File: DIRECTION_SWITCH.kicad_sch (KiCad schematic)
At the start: 0 parts

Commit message: Layout + Schematic weiter gemacht
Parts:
- added SW1: SW_Omron_B3FS, Button_Switch_SMD:SW_SPST_Omron_B3FS-105xP, symbol Switch:SW_Omron_B3FS
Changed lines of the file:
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@@
 		(rev "Rev 1")
 	)
+	(symbol
+		(lib_id "Switch:SW_Omron_B3FS")
+		(at 125.73 73.66 0)
+		(unit 1)
+		(body_style 1)
+		(exclude_from_sim no)
+		(in_bom yes)
+		(on_board yes)
+		(in_pos_files yes)
+		(dnp no)
+		(fields_autoplaced yes)
+		(property "Reference" "SW1"
+			(at 125.73 66.04 0)
+			(show_name no)
+			(do_not_autoplace no)
+			(effects
+				(font
+					(size 1.27 1.27)
+				)
+			)
+		)
+		(property "Value" "SW_Omron_B3FS"
+			(at 125.73 68.58 0)
+			(show_name no)
+			(do_not_autoplace no)
+			(effects
+				(font
+					(size 1.27 1.27)
+				)
+			)
+		)
+		(property "Footprint" "Button_Switch_SMD:SW_SPST_Omron_B3FS-105xP"
+			(at 125.73 68.58 0)
+			(hide yes)
+			(show_name no)
+			(do_not_autoplace no)
+			(effects
+				(font
+					(size 1.27 1.27)
+				)
+			)
+		)
+		(property "Datasheet" "https://omronfs.omron.com/en_US/ecb/products/pdf/en-b3fs.pdf"
+			(at 125.73 68.58 0)
+			(hide yes)
+			(show_name no)
+			(do_not_autoplace no)
+			(effects
+				(font
+					(size 1.27 1.27)
+				)
+			)
+		)
+		(property "Description" "Omron B3FS 6x6mm single pole normally-open tactile switch"
+			(at 125.73 73.66 0)
+			(hide yes)
+			(show_name no)
+			(do_not_autoplace no)
+			(effects
+				(font
+					(size 1.27 1.27)
+				)
+			)
+		)
+		(pin "1"
+		)
+		(pin "2"
+		)
+		(instances
+			(project ""
+				(path "/96aa4cdc-6548-43b6-b96a-6d1618c17d83/d0a02d27-ba8e-47f5-91ea-312e7e888d13"
+					(reference "SW1")
+					(unit 1)
+				)
+			)
+		)
+	)
 )

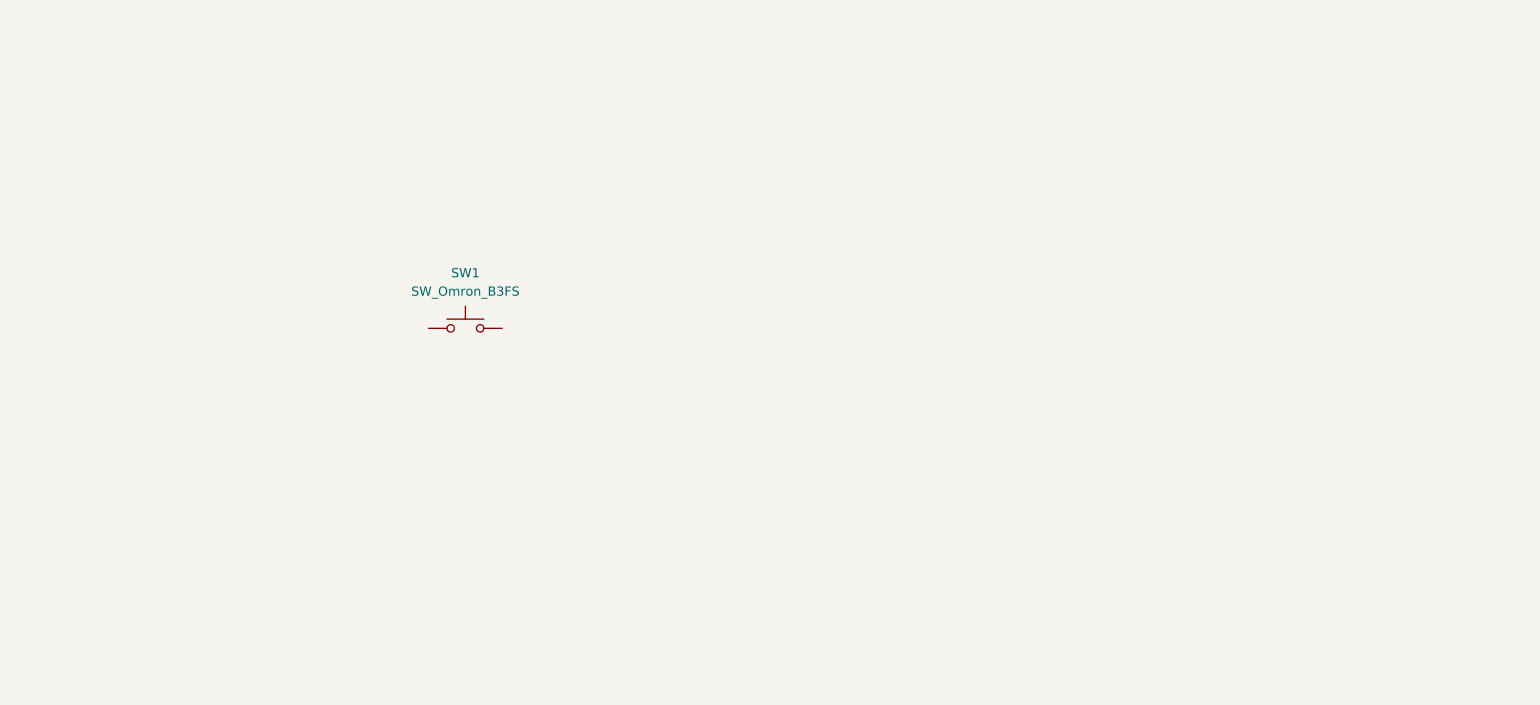
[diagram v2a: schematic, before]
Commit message: Button & Power Sequencing + Layout
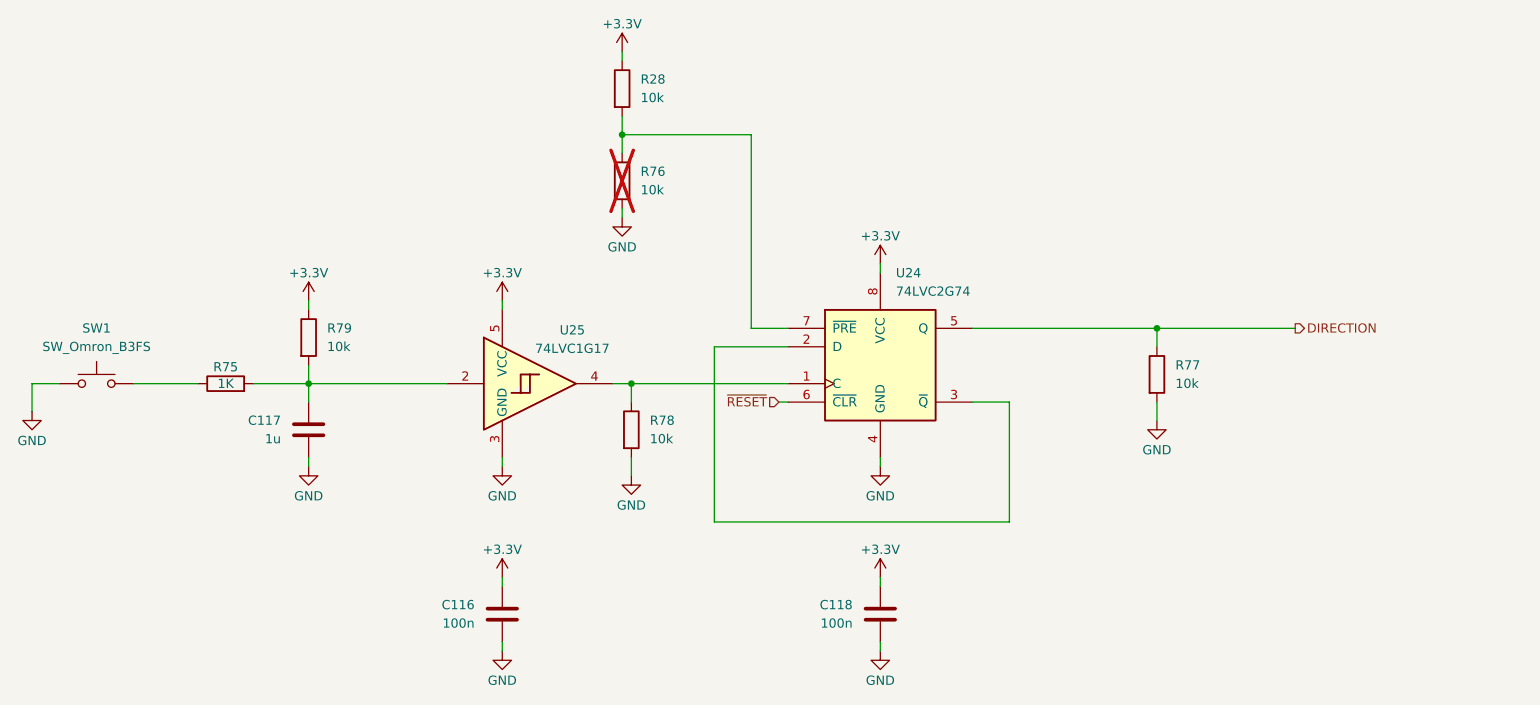
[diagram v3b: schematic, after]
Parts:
- added C116, C118: 100n, 00_Capacitor:Cap_0402, symbol Device:C
- added C117: 1u, 00_Capacitor:Cap_0402, symbol Device:C
- added R28, R76, R77, R78, R79: 10k, 00_Resistor:Res_0402, symbol Device:R
- added R75: 1K, 00_Capacitor:Cap_0402, symbol Device:R
- added U24: 74LVC2G74, 00_IC_Package_Misc:SOP50P310X90-8N, symbol 74xGxx:74LVC2G74
- added U25: 74LVC1G17, Package_TO_SOT_SMD:SOT-23-5, symbol 74xGxx:74LVC1G17
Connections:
- net GND: now reaches SW1.1
- net GND: now also C116.2, C117.2, C118.2, R76.2, R77.2, R78.2, U24.4 (GND), U25.3 (GND)
- net at SW1.2: now also R75.1
- new net: R28.2, R76.1, U24.7 (~{PRE})
- new net: C117.1, R75.2, R79.2, U25.2
- new net: R78.1, U24.1 (C), U25.4
- new net: U24.2 (D), U24.3 (~{Q})
- new net +3.3V: C116.1, C118.1, R28.1, R79.1, U24.8 (VCC), U25.5 (VCC)
- new net DIRECTION: R77.1, U24.5 (Q)
- new net ~{RESET}: U24.6 (~{CLR})
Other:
- moved on the sheet: SW1

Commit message: Layout nearly finished
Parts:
- added D3, D8: LED, LED_SMD:LED_0603_1608Metric, symbol Device:LED
- added R82, R83: 220, 00_Resistor:Res_0402, symbol Device:R
- R77: now not fitted
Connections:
- net +3.3V: now also R83.1
- net DIRECTION: now also D8.2 (A), R82.1
- net GND: now also D3.1 (K)
- new net: D8.1 (K), R83.2
- new net: D3.2 (A), R82.2
